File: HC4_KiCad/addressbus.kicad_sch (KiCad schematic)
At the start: 2 parts, among them IC15 74HC257, IC16 74HC257

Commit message: I'm tired. あとは任せた　頑張りたまえ
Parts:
- added CP13, CP14, CP15: 0.1u, Capacitor_THT:C_Disc_D3.0mm_W1.6mm_P2.50mm, symbol Device2:C_Bypass
- added IC18: 74HC00, symbol 74xx_2:74HC00
- added LD18, LD19, LD20, LD21, LD22, LD23, LD24, LD25: LED, LED_THT:LED_Rectangular_W5.0mm_H2.0mm, symbol Device2:LED_
- added R2: 10k, Resistor_THT:R_Axial_DIN0207_L6.3mm_D2.5mm_P7.62mm_Horizontal, symbol Device:R
- added RN5: 1k, Resistor_THT:R_Array_SIP9, symbol Device:R_Network08_Split
- added SW2: Bus_Open, Button_Switch_THT:SW_Slide-03_Wuerth-WS-SLTV_10x2.5x6.4_P2.54mm, symbol Switch:SW_SPDT
- renumbered IC15 to IC16, IC16 to IC17
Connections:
- net MEMMode: now reaches IC16.1 (S)
- net MEMMode: now also IC17.1 (S)
- net Level_B0: now reaches IC16.10 (I1d)
- net GND: now reaches IC16.11 (I0d)
- net GND: now also IC16.14 (I0c), IC16.2 (I0a), IC16.5 (I0b), IC16.8 (GND), IC17.8 (GND), CP13.2, CP14.2, CP15.2, IC18.7 (GND), R2.2, RN5.1 (R1), RN5.1 (R1), RN5.1 (R1), RN5.1 (R1), RN5.1 (R1), RN5.1 (R1), RN5.1 (R1), RN5.1 (R1)
- net RAM_A5: now reaches IC16.12 (Zc)
- net RAM_A5: now also LD20.2
- net Level_B1: now reaches IC16.13 (I1c)
- net at IC16.15 (OE): now also IC17.15 (OE), R2.1, SW2.2 (B)
- net VCC: now reaches IC16.16 (VCC)
- net VCC: now also IC17.16 (VCC), CP13.1, CP14.1, CP15.1, IC18.14 (VCC), SW2.1 (A)
- net Level_B3: now reaches IC16.3 (I1a)
- net RAM_A7: now reaches IC16.4 (Za)
- net RAM_A7: now also LD18.2
- net Level_B2: now reaches IC16.6 (I1b)
- net RAM_A6: now reaches IC16.7 (Zb)
- net RAM_A6: now also LD19.2
- net RAM_A4: now reaches IC16.9 (Zd)
- net RAM_A4: now also LD21.2
- net Level_A0: now reaches IC17.10 (I1d)
- net Instruction_0: now reaches IC17.11 (I0d)
- net RAM_A1: now reaches IC17.12 (Zc)
- net RAM_A1: now also LD24.2
- net Level_A1: now reaches IC17.13 (I1c)
- net Instruction_1: now reaches IC17.14 (I0c)
- net Instruction_3: now reaches IC17.2 (I0a)
- net Level_A3: now reaches IC17.3 (I1a)
- net RAM_A3: now reaches IC17.4 (Za)
- net RAM_A3: now also LD22.2
- net Instruction_2: now reaches IC17.5 (I0b)
- net Level_A2: now reaches IC17.6 (I1b)
- net RAM_A2: now reaches IC17.7 (Zb)
- net RAM_A2: now also LD23.2
- net RAM_A0: now reaches IC17.9 (Zd)
- net RAM_A0: now also LD25.2
- new net: LD24.1 (K), RN5.8 (R7.2)
- new net: LD18.1 (K), RN5.2 (R1.2)
- new net: LD21.1 (K), RN5.5 (R4.2)
- new net: LD22.1 (K), RN5.6 (R5.2)
- new net: LD25.1 (K), RN5.9 (R8.2)
- new net: LD19.1 (K), RN5.3 (R2.2)
- new net: LD20.1 (K), RN5.4 (R3.2)
- new net: LD23.1 (K), RN5.7 (R6.2)
- new net CLK2: IC18.2, IC18.5
- new net Instruction_7: IC18.4
- new net READ: IC18.1
- new net ~{RAM_RD}: IC18.3
- new net ~{RAM_WR}: IC18.6
- no-connect marks 0 -> 1
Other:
- note added: "WRITE"
- title: (none) -> CPU

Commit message: 回路図の修正
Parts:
- renumbered LD18 to LD20, LD19 to LD21, LD20 to LD22, LD21 to LD23, LD22 to LD24, LD23 to LD25, LD24 to LD26, LD25 to LD27, R2 to R4
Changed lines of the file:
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@@
 		(on_board yes)
 		(dnp no)
-		(property "Reference" "#PWR058"
+		(property "Reference" "#PWR059"
 			(at 148.59 200.66 0)
 			(effects
@@
 			(project ""
 				(path "/33731ded-38c0-4297-bdd8-92b082f46ff8/06be0d13-f4ff-478c-92b4-64c4ff1b6880"
-					(reference "#PWR058")
+					(reference "#PWR059")
 					(unit 1)
 				)
@@
 		(dnp no)
 		(fields_autoplaced yes)
-		(property "Reference" "LD18"
+		(property "Reference" "LD20"
 			(at 154.94 145.0974 90)
 			(effects
@@
 			(project "HC4_KiCad"
 				(path "/33731ded-38c0-4297-bdd8-92b082f46ff8/06be0d13-f4ff-478c-92b4-64c4ff1b6880"
-					(reference "LD18")
+					(reference "LD20")
 					(unit 1)
 				)
@@
 		(dnp no)
 		(fields_autoplaced yes)
-		(property "Reference" "LD21"
+		(property "Reference" "LD23"
 			(at 181.61 145.0974 90)
 			(effects
@@
 			(project "HC4_KiCad"
 				(path "/33731ded-38c0-4297-bdd8-92b082f46ff8/06be0d13-f4ff-478c-92b4-64c4ff1b6880"
-					(reference "LD21")
+					(reference "LD23")
 					(unit 1)
 				)
@@
 		(dnp no)
 		(fields_autoplaced yes)
-		(property "Reference" "#PWR054"
+		(property "Reference" "#PWR055"
 			(at 121.92 59.69 0)
 			(effects
@@
 			(project ""
 				(path "/33731ded-38c0-4297-bdd8-92b082f46ff8/06be0d13-f4ff-478c-92b4-64c4ff1b6880"
-					(reference "#PWR054")
+					(reference "#PWR055")
 					(unit 1)
 				)
@@
 		(dnp no)
 		(fields_autoplaced yes)
-		(property "Reference" "LD25"
+		(property "Reference" "LD27"
 			(at 218.44 145.0974 90)
 			(effects
@@
 			(project "HC4_KiCad"
 				(path "/33731ded-38c0-4297-bdd8-92b082f46ff8/06be0d13-f4ff-478c-92b4-64c4ff1b6880"
-					(reference "LD25")
+					(reference "LD27")
 					(unit 1)
 				)
@@
 		(dnp no)
 		(fields_autoplaced yes)
-		(property "Reference" "#PWR055"
+		(property "Reference" "#PWR056"
 			(at 121.92 114.3 0)
 			(effects
@@
 			(project ""
 				(path "/33731ded-38c0-4297-bdd8-92b082f46ff8/06be0d13-f4ff-478c-92b4-64c4ff1b6880"
-					(reference "#PWR055")
+					(reference "#PWR056")
 					(unit 1)
 				)
@@
 		(dnp no)
 		(fields_autoplaced yes)
-		(property "Reference" "LD24"
+		(property "Reference" "LD26"
 			(at 209.55 145.0974 90)
 			(effects
@@
 			(project "HC4_KiCad"
 				(path "/33731ded-38c0-4297-bdd8-92b082f46ff8/06be0d13-f4ff-478c-92b4-64c4ff1b6880"
-					(reference "LD24")
+					(reference "LD26")
 					(unit 1)
 				)
@@
 		(dnp no)
 		(fields_autoplaced yes)
-		(property "Reference" "LD20"
+		(property "Reference" "LD22"
 			(at 172.72 145.0974 90)
 			(effects
@@
 			(project "HC4_KiCad"
 				(path "/33731ded-38c0-4297-bdd8-92b082f46ff8/06be0d13-f4ff-478c-92b4-64c4ff1b6880"
-					(reference "LD20")
+					(reference "LD22")
 					(unit 1)
 				)
@@
 		(dnp no)
 		(fields_autoplaced yes)
-		(property "Reference" "R2"
+		(property "Reference" "R4"
 			(at 92.71 181.6099 0)
 			(effects
@@
 			(project ""
 				(path "/33731ded-38c0-4297-bdd8-92b082f46ff8/06be0d13-f4ff-478c-92b4-64c4ff1b6880"
-					(reference "R2")
+					(reference "R4")
 					(unit 1)
 				)
@@
 		(on_board yes)
 		(dnp no)
-		(property "Reference" "#PWR059"
+		(property "Reference" "#PWR060"
 			(at 149.86 172.72 0)
 			(effects
@@
 			(project ""
 				(path "/33731ded-38c0-4297-bdd8-92b082f46ff8/06be0d13-f4ff-478c-92b4-64c4ff1b6880"
-					(reference "#PWR059")
+					(reference "#PWR060")
 					(unit 1)
 				)
@@
 		(dnp no)
 		(fields_autoplaced yes)
-		(property "Reference" "LD19"
+		(property "Reference" "LD21"
 			(at 163.83 145.0974 90)
 			(effects
@@
 			(project "HC4_KiCad"
 				(path "/33731ded-38c0-4297-bdd8-92b082f46ff8/06be0d13-f4ff-478c-92b4-64c4ff1b6880"
-					(reference "LD19")
+					(reference "LD21")
 					(unit 1)
 				)
@@
 		(dnp no)
 		(fields_autoplaced yes)
-		(property "Reference" "#PWR060"
+		(property "Reference" "#PWR061"
 			(at 168.91 166.37 0)
 			(effects
@@
 			(project ""
 				(path "/33731ded-38c0-4297-bdd8-92b082f46ff8/06be0d13-f4ff-478c-92b4-64c4ff1b6880"
-					(reference "#PWR060")
+					(reference "#PWR061")
 					(unit 1)
 				)
@@
 		(dnp no)
 		(fields_autoplaced yes)
-		(property "Reference" "#PWR053"
+		(property "Reference" "#PWR054"
 			(at 90.17 196.85 0)
 			(effects
@@
 			(project ""
 				(path "/33731ded-38c0-4297-bdd8-92b082f46ff8/06be0d13-f4ff-478c-92b4-64c4ff1b6880"
-					(reference "#PWR053")
+					(reference "#PWR054")
 					(unit 1)
 				)
@@
 		(dnp no)
 		(fields_autoplaced yes)
-		(property "Reference" "LD23"
+		(property "Reference" "LD25"
 			(at 200.66 145.0974 90)
 			(effects
@@
 			(project "HC4_KiCad"
 				(path "/33731ded-38c0-4297-bdd8-92b082f46ff8/06be0d13-f4ff-478c-92b4-64c4ff1b6880"
-					(reference "LD23")
+					(reference "LD25")
 					(unit 1)
 				)
@@
 		(dnp no)
 		(fields_autoplaced yes)
-		(property "Reference" "#PWR056"
+		(property "Reference" "#PWR057"
 			(at 121.92 125.73 0)
 			(effects
@@
 			(project ""
 				(path "/33731ded-38c0-4297-bdd8-92b082f46ff8/06be0d13-f4ff-478c-92b4-64c4ff1b6880"
-					(reference "#PWR056")
+					(reference "#PWR057")
 					(unit 1)
 				)
@@
 		(dnp no)
 		(fields_autoplaced yes)
-		(property "Reference" "LD22"
+		(property "Reference" "LD24"
 			(at 191.77 145.0974 90)
 			(effects
@@
 			(project "HC4_KiCad"
 				(path "/33731ded-38c0-4297-bdd8-92b082f46ff8/06be0d13-f4ff-478c-92b4-64c4ff1b6880"
-					(reference "LD22")
+					(reference "LD24")
 					(unit 1)
 				)
@@
 		(dnp no)
 		(fields_autoplaced yes)
-		(property "Reference" "#PWR057"
+		(property "Reference" "#PWR058"
 			(at 121.92 179.07 0)
 			(effects
@@
 			(project ""
 				(path "/33731ded-38c0-4297-bdd8-92b082f46ff8/06be0d13-f4ff-478c-92b4-64c4ff1b6880"
-					(reference "#PWR057")
+					(reference "#PWR058")
 					(unit 1)
 				)
@@
 		(dnp no)
 		(fields_autoplaced yes)
-		(property "Reference" "#PWR052"
+		(property "Reference" "#PWR053"
 			(at 71.12 175.26 0)
 			(effects
@@
 			(project ""
 				(path "/33731ded-38c0-4297-bdd8-92b082f46ff8/06be0d13-f4ff-478c-92b4-64c4ff1b6880"
-					(reference "#PWR052")
+					(reference "#PWR053")
 					(unit 1)
 				)

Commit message: フットプリントの割り当て修正
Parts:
- IC16, IC17: footprint (none) -> Package_DIP:DIP-16_W7.62mm_Socket
- IC18: footprint (none) -> Package_DIP:DIP-14_W7.62mm_Socket
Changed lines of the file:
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@@
 	(label "Level_A3"
 		(at 96.52 133.35 0)
+		(fields_autoplaced yes)
 		(effects
 			(font
@@
 	(label "Instruction_1"
 		(at 96.52 146.05 0)
+		(fields_autoplaced yes)
 		(effects
 			(font
@@
 	(label "Instruction_0"
 		(at 96.52 153.67 0)
+		(fields_autoplaced yes)
 		(effects
 			(font
@@
 	(label "RAM_A1"
 		(at 205.74 133.35 270)
+		(fields_autoplaced yes)
 		(effects
 			(font
@@
 	(label "RAM_A3"
 		(at 187.96 133.35 270)
+		(fields_autoplaced yes)
 		(effects
 			(font
@@
 	(label "Instruction_7"
 		(at 109.22 124.46 180)
+		(fields_autoplaced yes)
 		(effects
 			(font
@@
 	(label "Level_B1"
 		(at 91.44 82.55 0)
+		(fields_autoplaced yes)
 		(effects
 			(font
@@
 	(label "RAM_A2"
 		(at 142.24 138.43 180)
+		(fields_autoplaced yes)
 		(effects
 			(font
@@
 	(label "Level_B3"
 		(at 91.44 67.31 0)
+		(fields_autoplaced yes)
 		(effects
 			(font
@@
 	(label "Level_A1"
 		(at 96.52 148.59 0)
+		(fields_autoplaced yes)
 		(effects
 			(font
@@
 	(label "RAM_A7"
 		(at 151.13 133.35 270)
+		(fields_autoplaced yes)
 		(effects
 			(font
@@
 	(label "RAM_A3"
 		(at 142.24 130.81 180)
+		(fields_autoplaced yes)
 		(effects
 			(font
@@
 	(label "Level_B0"
 		(at 91.44 90.17 0)
+		(fields_autoplaced yes)
 		(effects
 			(font
@@
 	(label "RAM_A7"
 		(at 142.24 64.77 180)
+		(fields_autoplaced yes)
 		(effects
 			(font
@@
 	(label "Instruction_2"
 		(at 96.52 138.43 0)
+		(fields_autoplaced yes)
 		(effects
 			(font
@@
 	(label "RAM_A2"
 		(at 196.85 133.35 270)
+		(fields_autoplaced yes)
 		(effects
 			(font
@@
 	(label "RAM_A6"
 		(at 160.02 133.35 270)
+		(fields_autoplaced yes)
 		(effects
 			(font
@@
 	(label "Level_B2"
 		(at 91.44 74.93 0)
+		(fields_autoplaced yes)
 		(effects
 			(font
@@
 	(label "RAM_A5"
 		(at 168.91 133.35 270)
+		(fields_autoplaced yes)
 		(effects
 			(font
@@
 	(label "RAM_A0"
 		(at 142.24 153.67 180)
+		(fields_autoplaced yes)
 		(effects
 			(font
@@
 	(label "RAM_A5"
 		(at 142.24 80.01 180)
+		(fields_autoplaced yes)
 		(effects
 			(font
@@
 	(label "RAM_A4"
 		(at 177.8 133.35 270)
+		(fields_autoplaced yes)
 		(effects
 			(font
@@
 	(label "RAM_A6"
 		(at 142.24 72.39 180)
+		(fields_autoplaced yes)
 		(effects
 			(font
@@
 	(label "Instruction_3"
 		(at 96.52 130.81 0)
+		(fields_autoplaced yes)
 		(effects
 			(font
@@
 	(label "Level_A0"
 		(at 96.52 156.21 0)
+		(fields_autoplaced yes)
 		(effects
 			(font
@@
 	(label "Level_A2"
 		(at 96.52 140.97 0)
+		(fields_autoplaced yes)
 		(effects
 			(font
@@
 	(label "RAM_A4"
 		(at 142.24 87.63 180)
+		(fields_autoplaced yes)
 		(effects
 			(font
@@
 	(label "RAM_A0"
 		(at 214.63 133.35 270)
+		(fields_autoplaced yes)
 		(effects
 			(font
@@
 	(label "RAM_A1"
 		(at 142.24 146.05 180)
+		(fields_autoplaced yes)
 		(effects
 			(font
@@
 		(shape input)
 		(at 106.68 95.25 180)
+		(fields_autoplaced yes)
 		(effects
 			(font
@@
 		(shape output)
 		(at 226.06 113.03 0)
+		(fields_autoplaced yes)
 		(effects
 			(font
@@
 		(shape input)
 		(at 82.55 129.54 180)
+		(fields_autoplaced yes)
 		(effects
 			(font
@@
 		(shape output)
 		(at 148.59 60.96 0)
+		(fields_autoplaced yes)
 		(effects
 			(font
@@
 		(shape input)
 		(at 105.41 161.29 180)
+		(fields_autoplaced yes)
 		(effects
 			(font
@@
 		(shape output)
 		(at 226.06 97.79 0)
+		(fields_autoplaced yes)
 		(effects
 			(font
@@
 		(shape input)
 		(at 86.36 63.5 180)
+		(fields_autoplaced yes)
 		(effects
 			(font
@@
 		(shape input)
 		(at 87.63 127 180)
+		(fields_autoplaced yes)
 		(effects
 			(font
@@
 		(shape input)
 		(at 198.12 95.25 180)
+		(fields_autoplaced yes)
 		(effects
 			(font
@@
 			)
 		)
-		(property "Footprint" ""
+		(property "Footprint" "Package_DIP:DIP-14_W7.62mm_Socket"
 			(at 215.9 97.79 0)
 			(effects
@@
 			)
 		)
-		(property "Footprint" ""
+		(property "Footprint" "Package_DIP:DIP-16_W7.62mm_Socket"
 			(at 121.92 80.01 0)
 			(effects
@@
 			)
 		)
-		(property "Footprint" ""
+		(property "Footprint" "Package_DIP:DIP-14_W7.62mm_Socket"
 			(at 161.29 181.61 0)
 			(effects
@@
 			)
 		)
-		(property "Footprint" ""
+		(property "Footprint" "Package_DIP:DIP-16_W7.62mm_Socket"
 			(at 121.92 146.05 0)
 			(effects
@@
 			)
 		)
-		(property "Footprint" ""
+		(property "Footprint" "Package_DIP:DIP-14_W7.62mm_Socket"
 			(at 215.9 113.03 0)
 			(effects

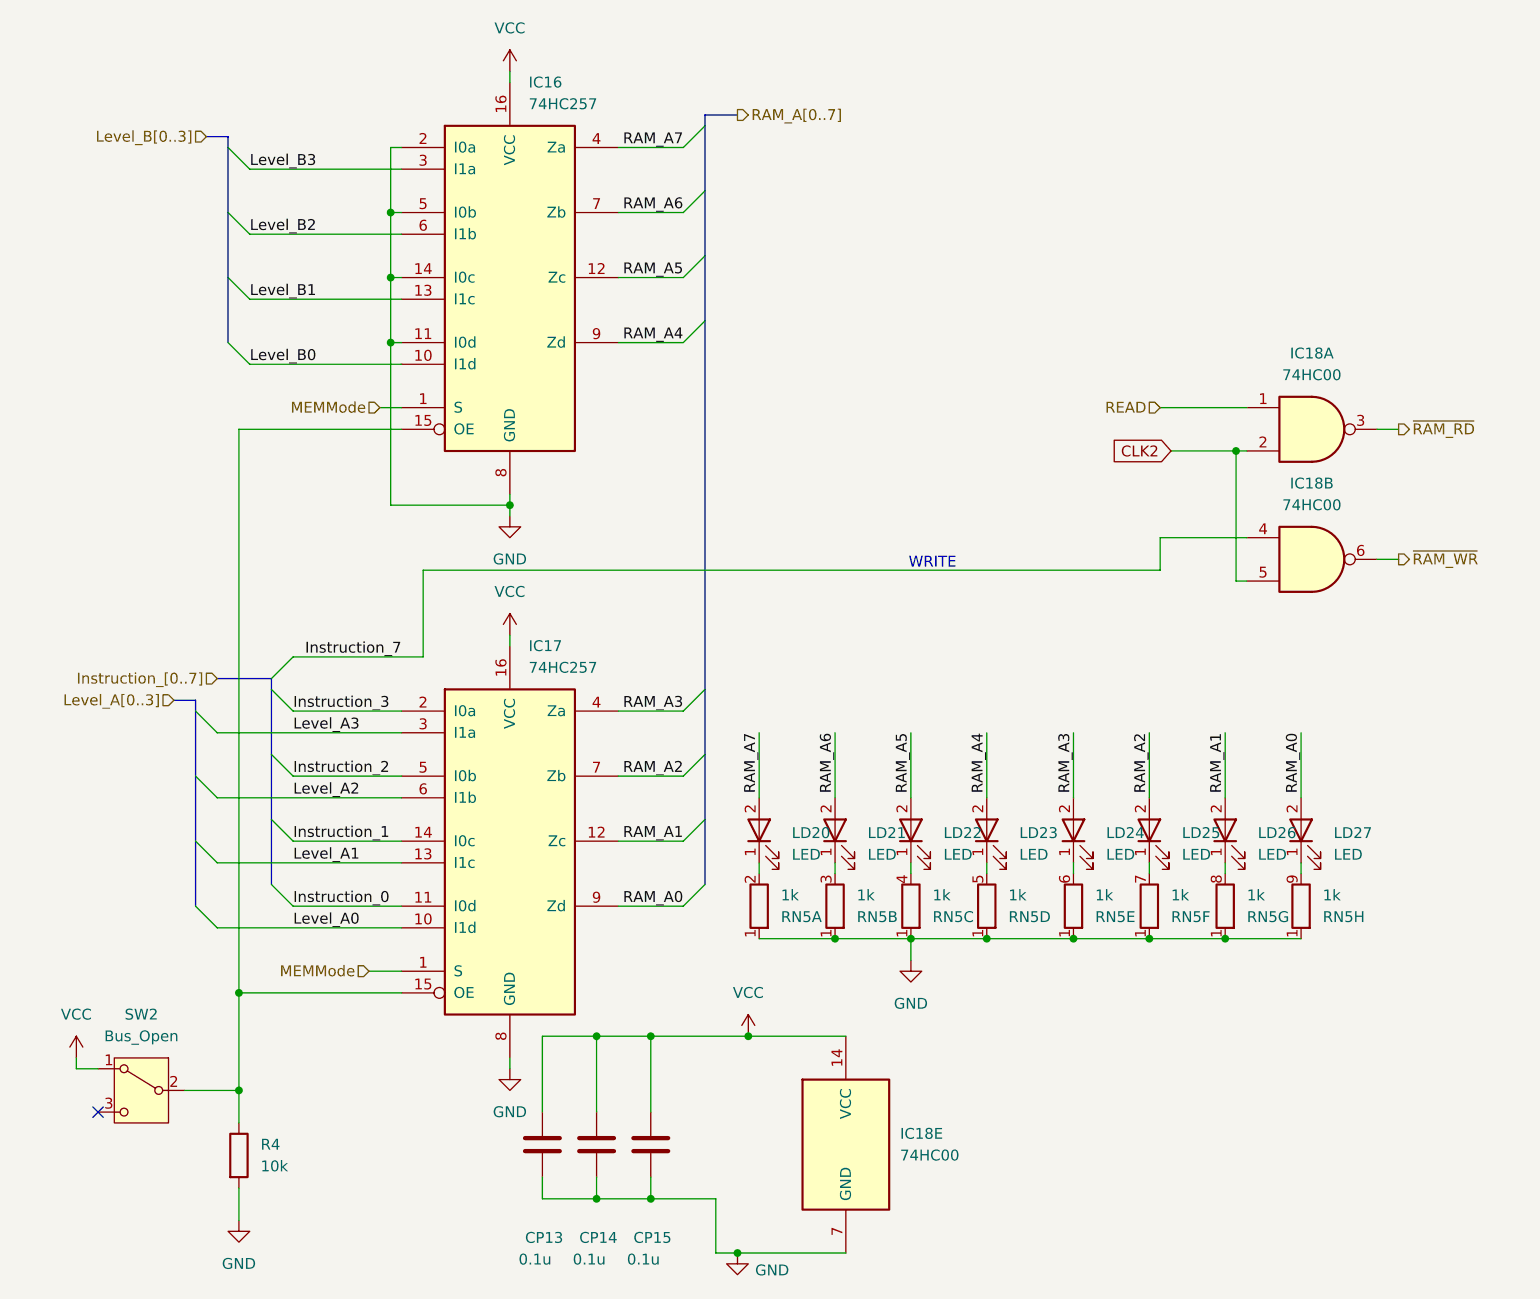
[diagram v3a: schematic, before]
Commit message: ICの配置を再検討
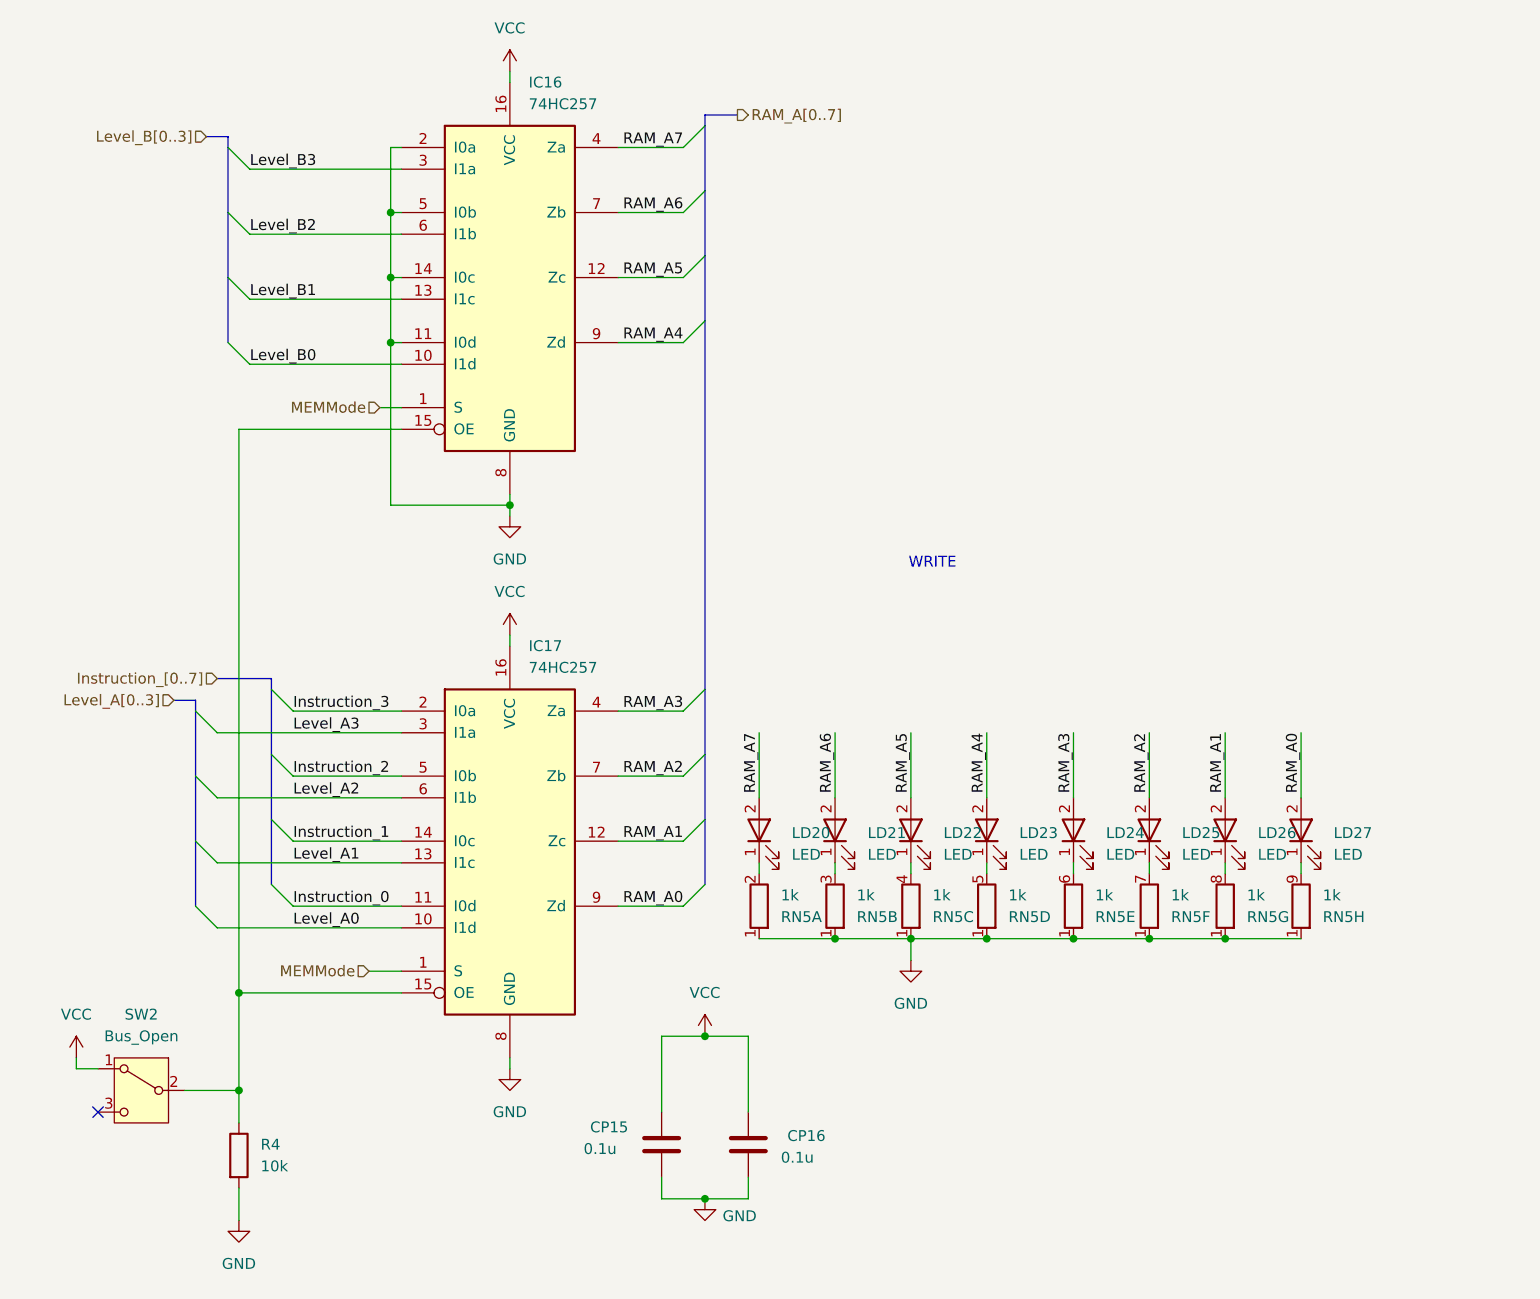
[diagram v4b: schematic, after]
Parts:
- removed CP15: 0.1u, Capacitor_THT:C_Disc_D3.0mm_W1.6mm_P2.50mm, symbol Device2:C_Bypass
- removed IC18: 74HC00, Package_DIP:DIP-14_W7.62mm_Socket, symbol 74xx_2:74HC00
- renumbered CP13 to CP15, CP14 to CP16
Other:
- moved on the sheet: CP15, CP16

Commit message: またも手直し
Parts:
- SW2: symbol Switch:SW_SPDT -> Switch:SW_SPDT_312
- renumbered LD20 to LD32, LD21 to LD33, LD22 to LD34, LD23 to LD35, LD24 to LD36, LD25 to LD37, LD26 to LD38, LD27 to LD39, RN5 to RN7
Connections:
- net VCC: now also SW2.3 (A); no longer SW2.1 (A)
- net at IC16.15 (OE), IC17.15 (OE), R4.1: now also SW2.1 (B); no longer SW2.2 (B)
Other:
- title: CPU -> HC4_CPU
